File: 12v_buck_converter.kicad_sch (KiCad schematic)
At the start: 23 parts, among them IC1 TPS56A37RPAR, Q4 BUK9K52-60RAX

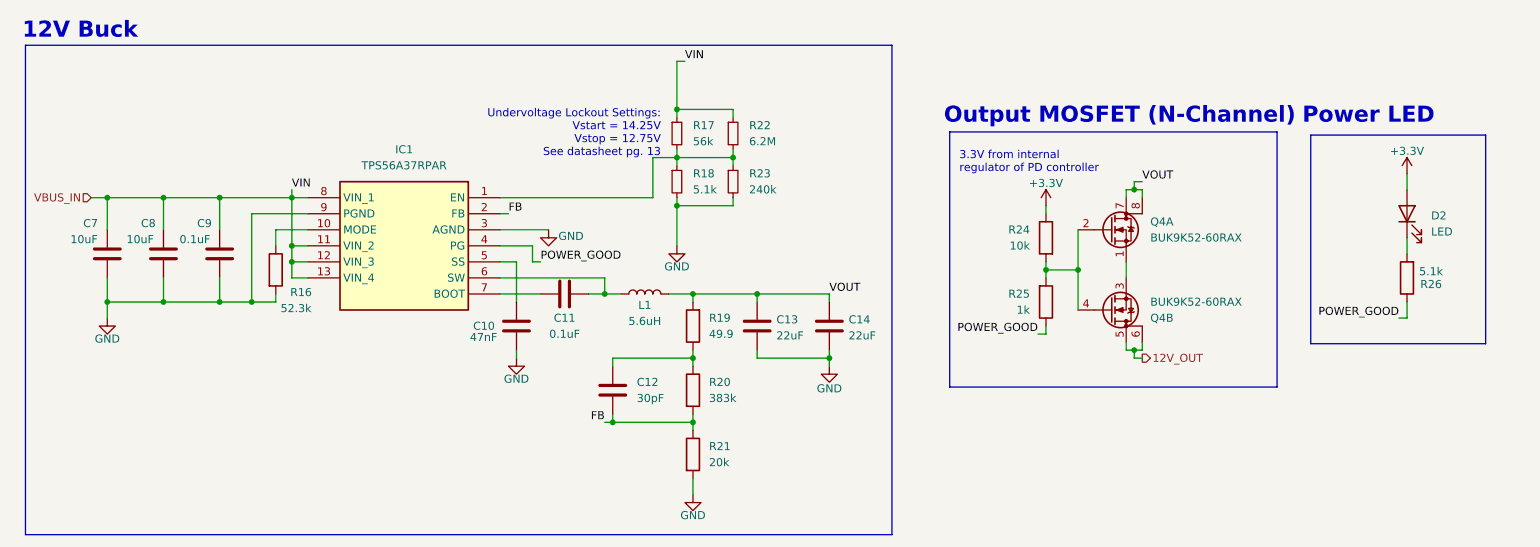
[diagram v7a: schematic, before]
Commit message: cleaned up schematic, added power LEDs and testpoints
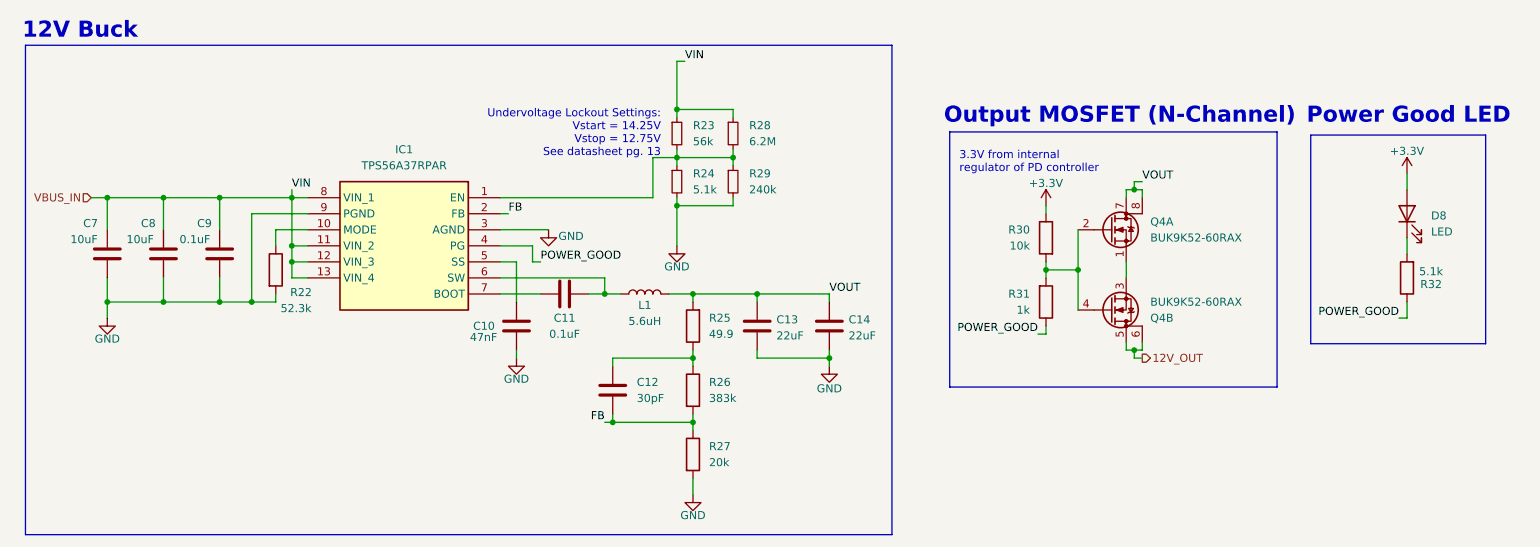
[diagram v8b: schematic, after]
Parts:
- D8: renamed from D2; If (none) -> 2mA; Vf (none) -> 1.9V
- renumbered R16 to R22, R17 to R23, R18 to R24, R19 to R25, R20 to R26, R21 to R27, R22 to R28, R23 to R29, R24 to R30, R25 to R31, R26 to R32
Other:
- note added: "Power Good LED"
- note removed: "Power LED"
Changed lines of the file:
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@@
 		)
 	)
-	(text "Power LED"
-		(exclude_from_sim no)
-		(at 244.094 73.406 0)
+	(text "Power Good LED"
+		(exclude_from_sim no)
+		(at 250.444 73.406 0)
 		(effects
 			(font
@@
 		(dnp no)
 		(fields_autoplaced yes)
-		(property "Reference" "R20"
+		(property "Reference" "R26"
 			(at 139.7 115.5699 0)
 			(effects
@@
 			(project "USBCPowerPCB"
 				(path "/f58400c5-df4b-4929-8d2b-33c0fe23fcd9/01d27e83-9627-42d8-8cf9-628e44513f14"
-					(reference "R20")
+					(reference "R26")
 					(unit 1)
 				)
@@
 		(on_board yes)
 		(dnp no)
-		(property "Reference" "#PWR030"
+		(property "Reference" "#PWR036"
 			(at 250.19 86.36 0)
 			(effects
@@
 			(project "USBCPowerPCB"
 				(path "/f58400c5-df4b-4929-8d2b-33c0fe23fcd9/01d27e83-9627-42d8-8cf9-628e44513f14"
-					(reference "#PWR030")
+					(reference "#PWR036")
 					(unit 1)
 				)
@@
 		(on_board yes)
 		(dnp no)
-		(property "Reference" "R26"
+		(property "Reference" "R32"
 			(at 254 100.076 0)
 			(effects
@@
 			(project "USBCPowerPCB"
 				(path "/f58400c5-df4b-4929-8d2b-33c0fe23fcd9/01d27e83-9627-42d8-8cf9-628e44513f14"
-					(reference "R26")
+					(reference "R32")
 					(unit 1)
 				)
@@
 		(on_board yes)
 		(dnp no)
-		(property "Reference" "#PWR023"
+		(property "Reference" "#PWR029"
 			(at 44.45 111.76 0)
 			(effects
@@
 			(project "USBCPowerPCB"
 				(path "/f58400c5-df4b-4929-8d2b-33c0fe23fcd9/01d27e83-9627-42d8-8cf9-628e44513f14"
-					(reference "#PWR023")
+					(reference "#PWR029")
 					(unit 1)
 				)
@@
 		(dnp no)
 		(fields_autoplaced yes)
-		(property "Reference" "R17"
+		(property "Reference" "R23"
 			(at 137.16 74.9299 0)
 			(effects
@@
 			(project "USBCPowerPCB"
 				(path "/f58400c5-df4b-4929-8d2b-33c0fe23fcd9/01d27e83-9627-42d8-8cf9-628e44513f14"
-					(reference "R17")
+					(reference "R23")
 					(unit 1)
 				)
@@
 		(on_board yes)
 		(dnp no)
-		(property "Reference" "R16"
+		(property "Reference" "R22"
 			(at 73.406 101.346 0)
 			(effects
@@
 			(project "USBCPowerPCB"
 				(path "/f58400c5-df4b-4929-8d2b-33c0fe23fcd9/01d27e83-9627-42d8-8cf9-628e44513f14"
-					(reference "R16")
+					(reference "R22")
 					(unit 1)
 				)
@@
 		(dnp no)
 		(fields_autoplaced yes)
-		(property "Reference" "R23"
+		(property "Reference" "R29"
 			(at 146.05 82.5499 0)
 			(effects
@@
 			(project "USBCPowerPCB"
 				(path "/f58400c5-df4b-4929-8d2b-33c0fe23fcd9/01d27e83-9627-42d8-8cf9-628e44513f14"
-					(reference "R23")
+					(reference "R29")
 					(unit 1)
 				)
@@
 		(on_board yes)
 		(dnp no)
-		(property "Reference" "#PWR028"
+		(property "Reference" "#PWR034"
 			(at 158.75 119.38 0)
 			(effects
@@
 			(project "USBCPowerPCB"
 				(path "/f58400c5-df4b-4929-8d2b-33c0fe23fcd9/01d27e83-9627-42d8-8cf9-628e44513f14"
-					(reference "#PWR028")
+					(reference "#PWR034")
 					(unit 1)
 				)
@@
 		(dnp no)
 		(fields_autoplaced yes)
-		(property "Reference" "R22"
+		(property "Reference" "R28"
 			(at 146.05 74.9299 0)
 			(effects
@@
 			(project "USBCPowerPCB"
 				(path "/f58400c5-df4b-4929-8d2b-33c0fe23fcd9/01d27e83-9627-42d8-8cf9-628e44513f14"
-					(reference "R22")
+					(reference "R28")
 					(unit 1)
 				)
@@
 		(dnp no)
 		(fields_autoplaced yes)
-		(property "Reference" "R18"
+		(property "Reference" "R24"
 			(at 137.16 82.5499 0)
 			(effects
@@
 			(project "USBCPowerPCB"
 				(path "/f58400c5-df4b-4929-8d2b-33c0fe23fcd9/01d27e83-9627-42d8-8cf9-628e44513f14"
-					(reference "R18")
+					(reference "R24")
 					(unit 1)
 				)
@@
 		(dnp no)
 		(fields_autoplaced yes)
-		(property "Reference" "D2"
+		(property "Reference" "D8"
 			(at 254 89.2174 90)
 			(effects
@@
 			)
 		)
+		(property "Vf" "1.9V"
+			(at 250.19 88.9 90)
+			(effects
+				(font
+					(size 1.27 1.27)
+				)
+				(hide yes)
+			)
+		)
+		(property "If" "2mA"
+			(at 250.19 88.9 90)
+			(effects
+				(font
+					(size 1.27 1.27)
+				)
+				(hide yes)
+			)
+		)
 		(pin "2"
 		)
@@
 			(project "USBCPowerPCB"
 				(path "/f58400c5-df4b-4929-8d2b-33c0fe23fcd9/01d27e83-9627-42d8-8cf9-628e44513f14"
-					(reference "D2")
+					(reference "D8")
 					(unit 1)
 				)
@@
 		(dnp no)
 		(fields_autoplaced yes)
-		(property "Reference" "R19"
+		(property "Reference" "R25"
 			(at 139.7 105.4099 0)
 			(effects
@@
 			(project "USBCPowerPCB"
 				(path "/f58400c5-df4b-4929-8d2b-33c0fe23fcd9/01d27e83-9627-42d8-8cf9-628e44513f14"
-					(reference "R19")
+					(reference "R25")
 					(unit 1)
 				)
@@
 		(on_board yes)
 		(dnp no)
-		(property "Reference" "#PWR027"
+		(property "Reference" "#PWR033"
 			(at 137.16 139.7 0)
 			(effects
@@
 			(project "USBCPowerPCB"
 				(path "/f58400c5-df4b-4929-8d2b-33c0fe23fcd9/01d27e83-9627-42d8-8cf9-628e44513f14"
-					(reference "#PWR027")
+					(reference "#PWR033")
 					(unit 1)
 				)
@@
 		(on_board yes)
 		(dnp no)
-		(property "Reference" "R25"
+		(property "Reference" "R31"
 			(at 190.5 101.5999 0)
 			(effects
@@
 			(project "USBCPowerPCB"
 				(path "/f58400c5-df4b-4929-8d2b-33c0fe23fcd9/01d27e83-9627-42d8-8cf9-628e44513f14"
-					(reference "R25")
+					(reference "R31")
 					(unit 1)
 				)
@@
 		(dnp no)
 		(fields_autoplaced yes)
-		(property "Reference" "R24"
+		(property "Reference" "R30"
 			(at 190.5 91.4399 0)
 			(effects
@@
 			(project "USBCPowerPCB"
 				(path "/f58400c5-df4b-4929-8d2b-33c0fe23fcd9/01d27e83-9627-42d8-8cf9-628e44513f14"
-					(reference "R24")
+					(reference "R30")
 					(unit 1)
 				)
@@
 		(on_board yes)
 		(dnp no)
-		(property "Reference" "#PWR029"
+		(property "Reference" "#PWR035"
 			(at 193.04 91.44 0)
 			(effects
@@
 			(project "USBCPowerPCB"
 				(path "/f58400c5-df4b-4929-8d2b-33c0fe23fcd9/01d27e83-9627-42d8-8cf9-628e44513f14"
-					(reference "#PWR029")
+					(reference "#PWR035")
 					(unit 1)
 				)
@@
 		(on_board yes)
 		(dnp no)
-		(property "Reference" "#PWR024"
+		(property "Reference" "#PWR030"
 			(at 109.22 118.11 0)
 			(effects
@@
 			(project "USBCPowerPCB"
 				(path "/f58400c5-df4b-4929-8d2b-33c0fe23fcd9/01d27e83-9627-42d8-8cf9-628e44513f14"
-					(reference "#PWR024")
+					(reference "#PWR030")
 					(unit 1)
 				)
@@
 		(dnp no)
 		(fields_autoplaced yes)
-		(property "Reference" "R21"
+		(property "Reference" "R27"
 			(at 139.7 125.7299 0)
 			(effects
@@
 			(project "USBCPowerPCB"
 				(path "/f58400c5-df4b-4929-8d2b-33c0fe23fcd9/01d27e83-9627-42d8-8cf9-628e44513f14"
-					(reference "R21")
+					(reference "R27")
 					(unit 1)
 				)
@@
 		(on_board yes)
 		(dnp no)
-		(property "Reference" "#PWR026"
+		(property "Reference" "#PWR032"
 			(at 134.62 100.33 0)
 			(effects
@@
 			(project "USBCPowerPCB"
 				(path "/f58400c5-df4b-4929-8d2b-33c0fe23fcd9/01d27e83-9627-42d8-8cf9-628e44513f14"
-					(reference "#PWR026")
+					(reference "#PWR032")
 					(unit 1)
 				)
@@
 		(on_board yes)
 		(dnp no)
-		(property "Reference" "#PWR025"
+		(property "Reference" "#PWR031"
 			(at 114.3 97.79 0)
 			(effects
@@
 			(project "USBCPowerPCB"
 				(path "/f58400c5-df4b-4929-8d2b-33c0fe23fcd9/01d27e83-9627-42d8-8cf9-628e44513f14"
-					(reference "#PWR025")
-					(unit 1)
-				)
+					(reference "#PWR031")
+					(unit 1)
+				)
